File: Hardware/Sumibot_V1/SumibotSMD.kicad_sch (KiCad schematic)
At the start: 4 parts

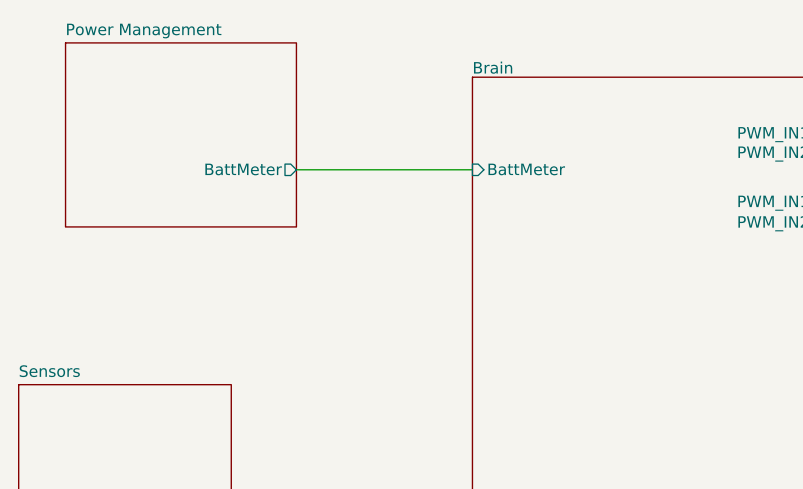
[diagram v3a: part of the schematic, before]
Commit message: implementó on/off toggle switch
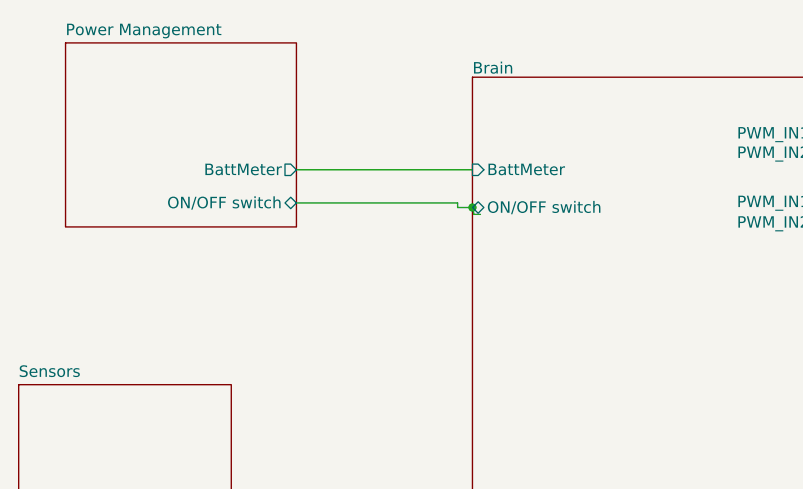
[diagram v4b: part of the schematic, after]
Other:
- sheet Brain ports: added ON/OFF switch; removed none
- sheet Power Management ports: added ON/OFF switch; removed none
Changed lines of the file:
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@@
     (comment 1 "Marcelo Ortiz")
   )
+  (junction (at 85.471 108.458) (diameter 0) (color 0 0 0 0)
+  )
+  (wire (pts (xy 85.471 108.458) (xy 85.598 108.458))
+    (stroke (width 0) (type default) (color 0 0 0 0))
+  )
   (bus (pts (xy 106.045 159.639) (xy 106.045 170.307))
     (stroke (width 0) (type default) (color 0 0 0 0))
@@
     (stroke (width 0) (type default) (color 0 0 0 0))
   )
+  (wire (pts (xy 66.04 107.95) (xy 83.82 107.95))
+    (stroke (width 0) (type default) (color 0 0 0 0))
+  )
+  (wire (pts (xy 83.82 108.458) (xy 85.471 108.458))
+    (stroke (width 0) (type default) (color 0 0 0 0))
+  )
   (wire (pts (xy 65.913 104.267) (xy 85.471 104.267))
     (stroke (width 0) (type default) (color 0 0 0 0))
@@
     (stroke (width 0) (type default) (color 0 0 0 0))
   )
+  (wire (pts (xy 85.598 108.458) (xy 85.598 109.22))
+    (stroke (width 0) (type default) (color 0 0 0 0))
+  )
   (wire (pts (xy 125.73 110.109) (xy 149.225 110.109))
     (stroke (width 0) (type default) (color 0 0 0 0))
   )
+  (wire (pts (xy 85.598 109.22) (xy 86.36 109.22))
+    (stroke (width 0) (type default) (color 0 0 0 0))
+  )
   (bus (pts (xy 58.547 170.053) (xy 106.045 170.307))
     (stroke (width 0) (type default) (color 0 0 0 0))
   )
+  (wire (pts (xy 83.82 107.95) (xy 83.82 108.458))
+    (stroke (width 0) (type default) (color 0 0 0 0))
+  )
   (symbol (lib_id "Mechanical:MountingHole") (at 70.612 255.651 0) (unit 1)
     (in_bom no) (on_board yes) (fields_autoplaced)
@@
       (effects (font (size 1.27 1.27)) (justify right))
     )
+    (pin "ON{slash}OFF switch" bidirectional (at 65.913 107.95 0)
+      (effects (font (size 1.27 1.27)) (justify right))
+    )
   )
   (sheet (at 149.225 93.98) (size 26.797 22.098) (fields_autoplaced)
@@
     )
     (pin "BattMeter" input (at 85.471 104.267 180)
+      (effects (font (size 1.27 1.27)) (justify left))
+    )
+    (pin "ON{slash}OFF switch" bidirectional (at 85.471 108.458 180)
       (effects (font (size 1.27 1.27)) (justify left))
     )
@@
       (reference "#FLG03") (unit 1) (value "PWR_FLAG") (footprint "")
     )
-    (path "/26f283ad-c3bb-41f7-a2c3-f3c93843d496/7dd68a6a-66d4-479c-810a-3b6f633d834d"
-      (reference "#FLG?") (unit 1) (value "PWR_FLAG") (footprint "")
-    )
     (path "/458205a8-00e8-4348-9aab-ba267ac5d6fd/f8df53e4-7969-40a1-a21c-0e61acb4a348"
